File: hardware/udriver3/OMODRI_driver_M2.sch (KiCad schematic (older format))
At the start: 46 parts, among them J12 Conn_01x03, Q4 CSD88599Q5DC, Q5 CSD88599Q5DC, Q6 CSD88599Q5DC, U20 DRV8353S

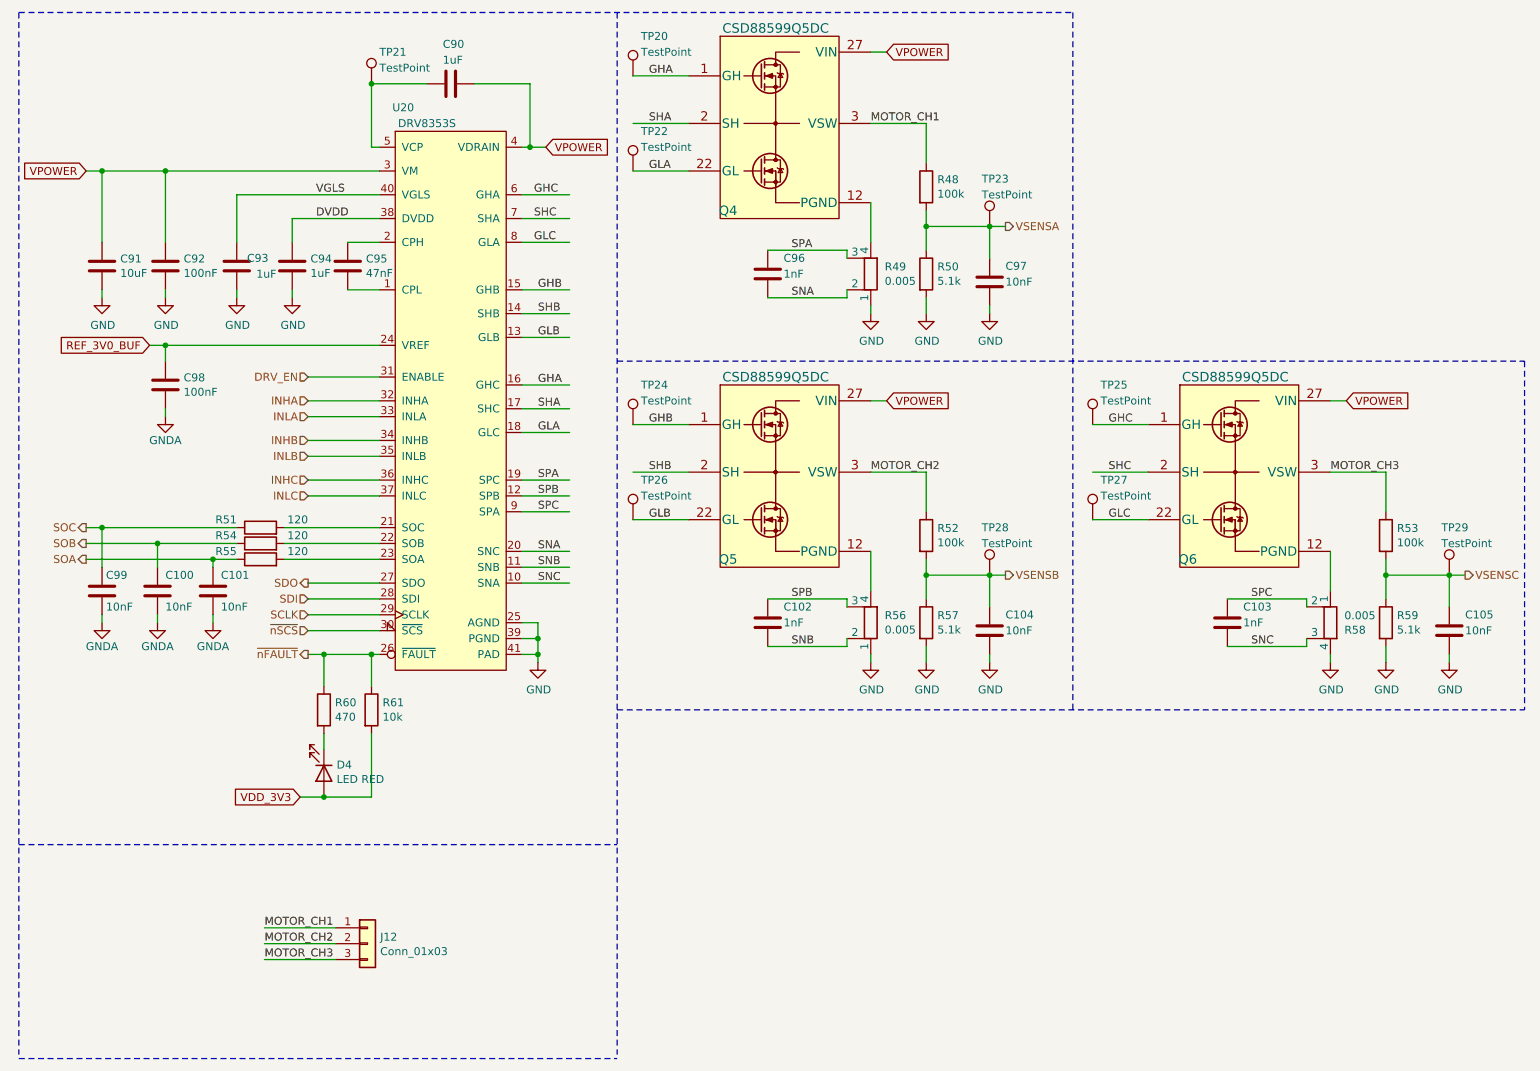
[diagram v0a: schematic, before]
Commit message: Update of the schematics. Switches on GPIO72 & GPIO84 are missing. J1, J2 & J14 must be merged and connector placement optimized. TCXO must be changed from 20MHz to 25MHz for EtherCAT compatibility. PCB is partially routed in 6-Layers (mainly power supplies and and transistors). 8-Layers will be necessary.
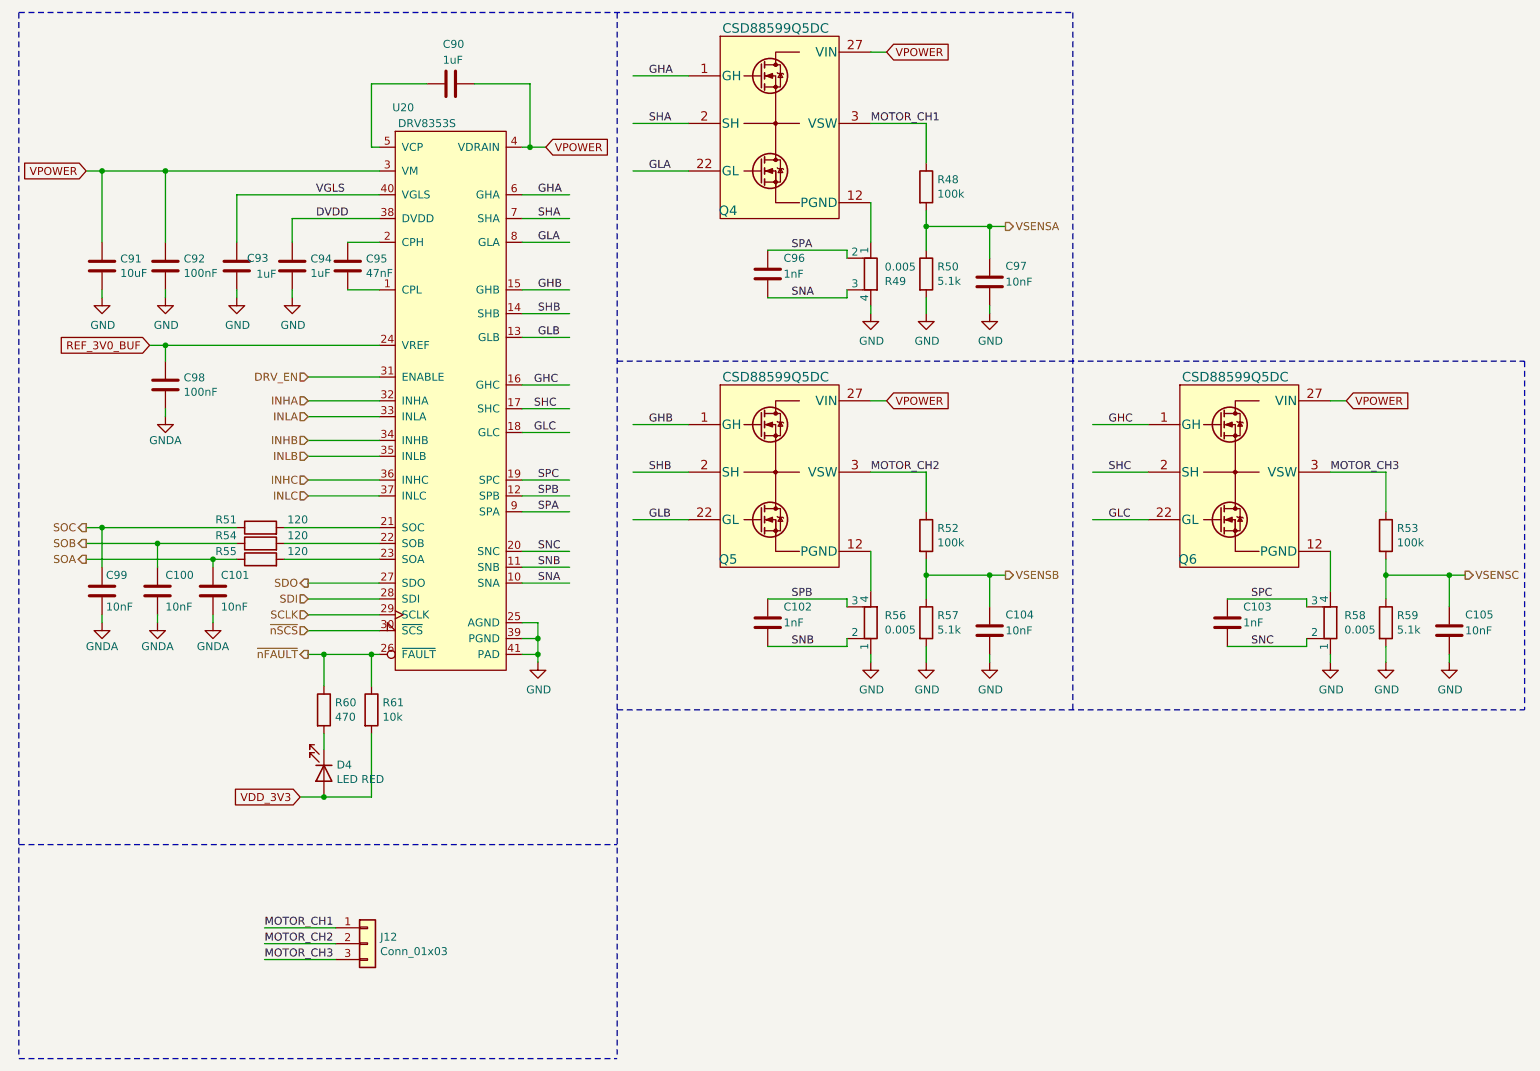
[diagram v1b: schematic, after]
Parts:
- removed TP20, TP21, TP22, TP23, TP24, TP25, TP26, TP27, TP28, TP29: TestPoint, TestPoint:TestPoint_Pad_D1.0mm, symbol Connector:TestPoint
- J12: footprint Connector_AMASS:AMASS_MR30PW-FB_1x03_P3.50mm_Horizontal -> udriver3:AMASS_MR30PW-FB_1x03_P3.50mm_Horizontal

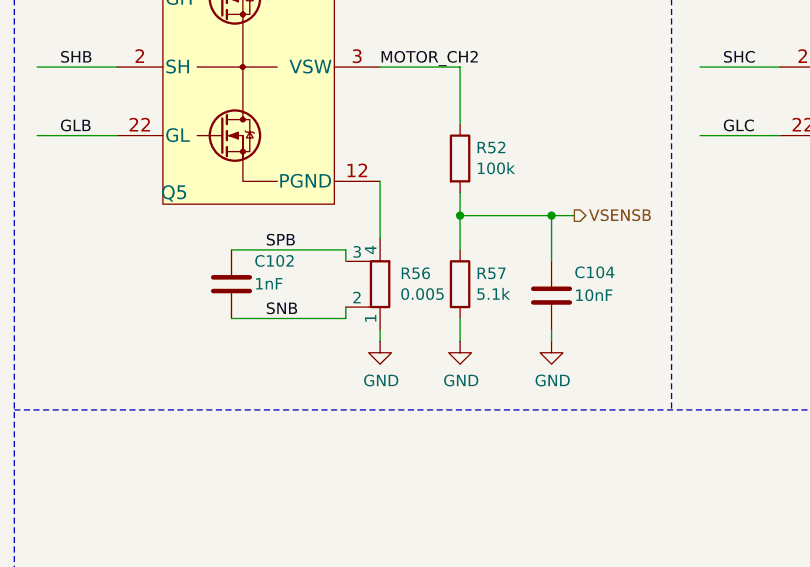
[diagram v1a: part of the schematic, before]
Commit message: Routing update. All analog and DRV signals are wired. TMS mcu decoupling capacitors are in place.
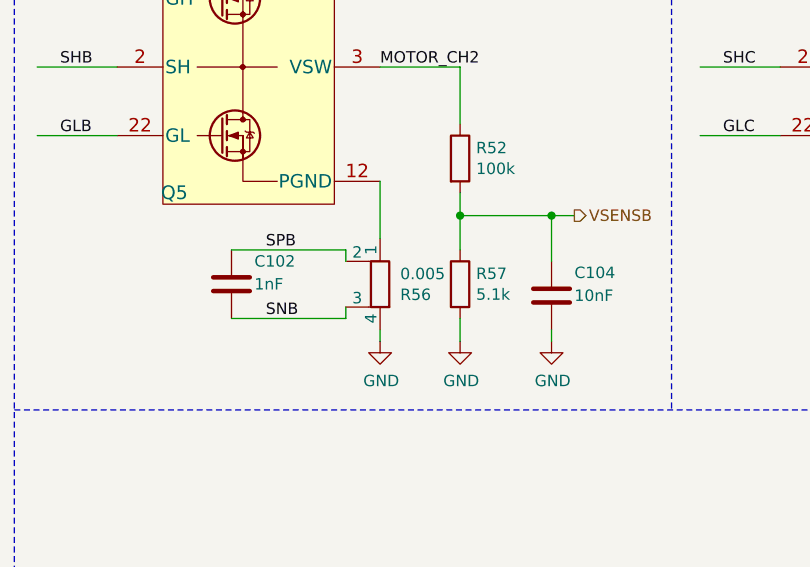
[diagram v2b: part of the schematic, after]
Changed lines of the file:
@@
-$EndComp
-$Comp
-L Device:R_Shunt R?
-U 1 1 5F80EF8F
-P 6025 2350
-AR Path="/5F310311/5F80EF8F" Ref="R?"  Part="1"
-AR Path="/5F3255E8/5F80EF8F" Ref="R?"  Part="1"
-AR Path="/5F387075/5F80EF8F" Ref="R?"  Part="1"
-AR Path="/5F5FCCBB/5F80EF8F" Ref="R?"  Part="1"
-AR Path="/5F71C92E/5F80EF8F" Ref="R49"  Part="1"
-F 0 "R49" H 5937 2304 50  0000 R CNN
-F 1 "0.005" H 5937 2395 50  0000 R CNN
-F 2 "udriver3:FC4L64" V 5955 2350 50  0001 C CNN
-F 3 "https://www.ohmite.com/assets/docs/res_fc4l.pdf?r=false" H 6025 2350 50  0001 C CNN
-F 4 "FC4L64R005FERCT-ND" H 6025 2350 50  0001 C CNN "DigiKey"
-F 5 "2363991" H 6025 2350 50  0001 C CNN "Farnell"
-F 6 "588-FC4L64R005FER" H 6025 2350 50  0001 C CNN "Mouser"
-F 7 "FC4L64R005FER" H 6025 2350 50  0001 C CNN "Part No"
-F 8 "126-0365" H 6025 2350 50  0001 C CNN "RS"
-	1    6025 2350
-	-1   0    0    -1
 $EndComp
 $Comp
@@
 F 8 "126-0365" H 6025 4550 50  0001 C CNN "RS"
 	1    6025 4550
-	-1   0    0    1
+	-1   0    0    -1
+$EndComp
+$Comp
+L Device:R_Shunt R?
+U 1 1 5F80EF8F
+P 6025 2350
+AR Path="/5F310311/5F80EF8F" Ref="R?"  Part="1"
+AR Path="/5F3255E8/5F80EF8F" Ref="R?"  Part="1"
+AR Path="/5F387075/5F80EF8F" Ref="R?"  Part="1"
+AR Path="/5F5FCCBB/5F80EF8F" Ref="R?"  Part="1"
+AR Path="/5F71C92E/5F80EF8F" Ref="R49"  Part="1"
+F 0 "R49" H 5937 2304 50  0000 R CNN
+F 1 "0.005" H 5937 2395 50  0000 R CNN
+F 2 "udriver3:FC4L64" V 5955 2350 50  0001 C CNN
+F 3 "https://www.ohmite.com/assets/docs/res_fc4l.pdf?r=false" H 6025 2350 50  0001 C CNN
+F 4 "FC4L64R005FERCT-ND" H 6025 2350 50  0001 C CNN "DigiKey"
+F 5 "2363991" H 6025 2350 50  0001 C CNN "Farnell"
+F 6 "588-FC4L64R005FER" H 6025 2350 50  0001 C CNN "Mouser"
+F 7 "FC4L64R005FER" H 6025 2350 50  0001 C CNN "Part No"
+F 8 "126-0365" H 6025 2350 50  0001 C CNN "RS"
+	1    6025 2350
+	-1   0    0    -1
 $EndComp
 $EndSCHEMATC

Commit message: First release of the fully routed OMODRI PCB from LAAS. (8 layers)
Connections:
- net labels added: CPH, CPL, OUT_M2_CH1, OUT_M2_CH2, OUT_M2_CH3, VCP_DRV
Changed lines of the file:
@@
 $Descr A4 11693 8268
 encoding utf-8
-Sheet 13 17
+Sheet 11 19
 Title "Open MOtor DRiver Initiative (OMODRI)"
 Date ""
@@
 	-1   0    0    -1
 $EndComp
+Text Label 2925 1150 0    50   ~ 0
+VCP_DRV
+Text Label 2750 2150 0    50   ~ 0
+CPH
+Text Label 2750 2450 0    50   ~ 0
+CPL
+Text Label 6025 2150 1    50   ~ 0
+OUT_M2_CH1
+Text Label 6025 4325 1    50   ~ 0
+OUT_M2_CH2
+Text Label 8925 4325 1    50   ~ 0
+OUT_M2_CH3
 $EndSCHEMATC

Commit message: Released version, with 4mils/4mils for track width and isolation on outer and inner layers 0.45mm for inner and outer annular ring 0.1mm for finished via drill (for Seeed studio increase to 0.2mm) + USB connector added
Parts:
- C92: footprint Capacitor_SMD:C_0805_2012Metric -> Capacitor_SMD:C_0603_1608Metric
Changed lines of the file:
@@
 F 0 "C92" H 1690 2346 50  0000 L CNN
 F 1 "100nF" H 1690 2255 50  0000 L CNN
-F 2 "Capacitor_SMD:C_0805_2012Metric" H 1613 2150 50  0001 C CNN
+F 2 "Capacitor_SMD:C_0603_1608Metric" H 1613 2150 50  0001 C CNN
 F 3 "https://www.murata.com/en-eu/products/productdetail?partno=GRM188R72A104KA35%23" H 1575 2300 50  0001 C CNN
 F 4 "" H 1575 2300 50  0001 C CNN "RS"

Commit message: Release 1.1 - Update components values + BOM - Update of J1 pins affectation now matching J2 distribution. - Update gerber files with missing inner layers - Few updates of the PCB layout (J2 redraw + decoupling cap)
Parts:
- C100, C101, C99: value 10nF -> 1.8nF; DigiKey 490-14454-1-ND -> 490-GRM033R71E182KA12DTR-ND; Farnell 2990696 -> 2999522; Mouser 81-GRM033R71E103KE4D -> 81-GRM033R71E182KA2D; Part No GRM033R71E103KE14D -> GRM033R71E182KA12D; RS 185-2059 -> (none)
- C102, C103, C96: value 1nF -> 1.8nF; DigiKey 490-10682-1-ND -> 490-GRM033R71E182KA12DTR-ND; Farnell 2990701 -> 2999522; Mouser 81-GRM033R71H102KA2D -> 81-GRM033R71E182KA2D; Part No GRM033R71H102KA12D -> GRM033R71E182KA12D; RS 185-2113 -> (none)
- C104, C105, C97: value 10nF -> 470nF; DigiKey 490-14454-1-ND -> 490-10410-1-ND; Farnell 2990696 -> 3243323; Mouser 81-GRM033R71E103KE4D -> 81-GRM33R60J474ME90D; Part No GRM033R71E103KE14D -> GRM033R60J474ME90D; RS 185-2059 -> 185-1791
- C98: DigiKey 490-14450-1-ND -> 490-14571-1-ND; Farnell 2990681 -> 3790414; Mouser 81-GRM033C71A104KE4D -> 81-GRM033R61E104KE4J; Part No GRM033C71A104KE14D -> GRM033R61E104KE14J; RS 185-1751 -> 185-2066
